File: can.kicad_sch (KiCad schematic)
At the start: 3 parts, among them J6 Conn_01x02, U6 TCAN334

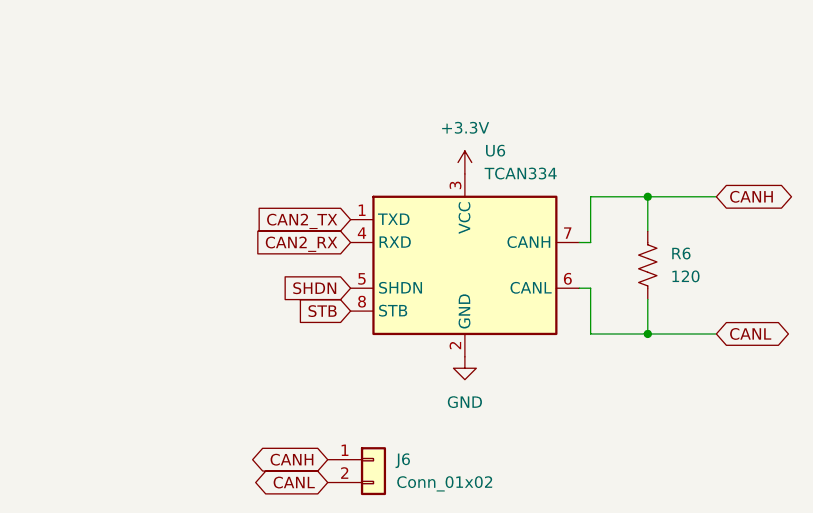
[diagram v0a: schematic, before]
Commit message: added load switches
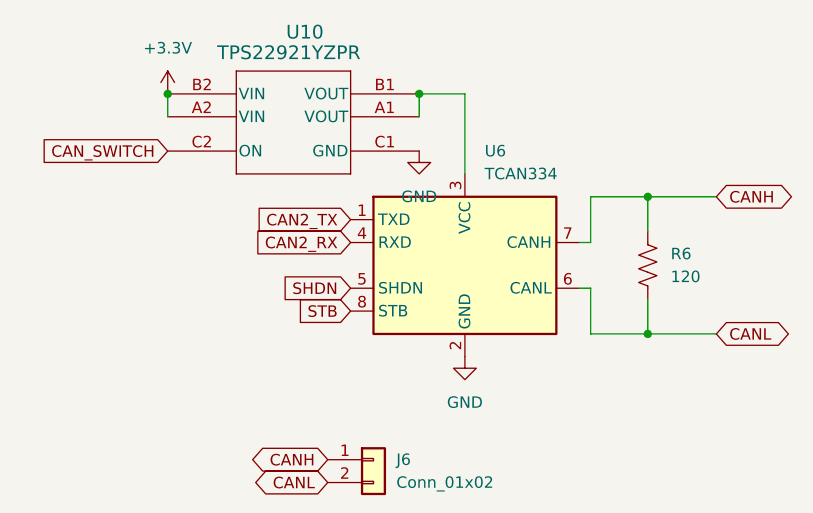
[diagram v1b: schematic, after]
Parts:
- added U10: TPS22921YZPR, YZP6, symbol TPS22921:TPS22921YZPR
- J6: footprint (none) -> Connector_JST:JST_SH_BM02B-SRSS-TB_1x02-1MP_P1.00mm_Vertical
- R6: footprint (none) -> Resistor_SMD:R_0402_1005Metric
- U6: footprint (none) -> footprints:DCN0008A_M
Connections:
- net +3.3V: now also U10.A2 (VIN), U10.B2 (VIN); no longer U6.3 (VCC)
- net GND: now also U10.C1 (GND)
- new net: U10.A1 (VOUT), U10.B1 (VOUT), U6.3 (VCC)
- new net CAN_SWITCH: U10.C2 (ON)
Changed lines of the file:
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@@
+	)
+	(junction
+		(at 29.21 35.56)
+		(diameter 0)
+		(color 0 0 0 0)
+	)
+	(junction
+		(at 57.15 35.56)
+		(diameter 0)
+		(color 0 0 0 0)
 	)
 	(junction
@@
 	(wire
 		(pts
+			(xy 57.15 35.56) (xy 57.15 38.1)
+		)
+		(stroke
+			(width 0)
+			(type default)
+		)
+	)
+	(wire
+		(pts
 			(xy 76.2 46.99) (xy 76.2 52.07)
 		)
@@
 	(wire
 		(pts
+			(xy 62.23 35.56) (xy 62.23 44.45)
+		)
+		(stroke
+			(width 0)
+			(type default)
+		)
+	)
+	(wire
+		(pts
+			(xy 57.15 35.56) (xy 62.23 35.56)
+		)
+		(stroke
+			(width 0)
+			(type default)
+		)
+	)
+	(wire
+		(pts
 			(xy 76.2 52.07) (xy 74.93 52.07)
 		)
@@
 		(pts
 			(xy 76.2 57.15) (xy 74.93 57.15)
+		)
+		(stroke
+			(width 0)
+			(type default)
+		)
+	)
+	(wire
+		(pts
+			(xy 29.21 35.56) (xy 29.21 38.1)
 		)
 		(stroke
@@
 		)
 	)
+	(global_label "CAN_SWITCH"
+		(shape input)
+		(at 29.21 41.91 180)
+		(fields_autoplaced yes)
+		(effects
+			(font
+				(size 1.27 1.27)
+			)
+			(justify right)
+		)
+		(property "Intersheetrefs" "${INTERSHEET_REFS}"
+			(at 14.7343 41.91 0)
+			(effects
+				(font
+					(size 1.27 1.27)
+				)
+				(justify right)
+				(hide yes)
+			)
+		)
+	)
 	(global_label "SHDN"
 		(shape input)
@@
 				)
 				(hide yes)
+			)
+		)
+	)
+	(symbol
+		(lib_id "power:GND")
+		(at 57.15 41.91 0)
+		(unit 1)
+		(exclude_from_sim no)
+		(in_bom yes)
+		(on_board yes)
+		(dnp no)
+		(fields_autoplaced yes)
+		(property "Reference" "#PWR060"
+			(at 57.15 48.26 0)
+			(effects
+				(font
+					(size 1.27 1.27)
+				)
+				(hide yes)
+			)
+		)
+		(property "Value" "GND"
+			(at 57.15 46.99 0)
+			(effects
+				(font
+					(size 1.27 1.27)
+				)
+			)
+		)
+		(property "Footprint" ""
+			(at 57.15 41.91 0)
+			(effects
+				(font
+					(size 1.27 1.27)
+				)
+				(hide yes)
+			)
+		)
+		(property "Datasheet" ""
+			(at 57.15 41.91 0)
+			(effects
+				(font
+					(size 1.27 1.27)
+				)
+				(hide yes)
+			)
+		)
+		(property "Description" "Power symbol creates a global label with name \"GND\" , ground"
+			(at 57.15 41.91 0)
+			(effects
+				(font
+					(size 1.27 1.27)
+				)
+				(hide yes)
+			)
+		)
+		(pin "1"
+		)
+		(instances
+			(project "RT1050"
+				(path "/dd9d031d-43a1-4442-b493-27451a14e0d9/1717ddd0-007d-45d1-b2d6-3a5f196579be"
+					(reference "#PWR060")
+					(unit 1)
+				)
 			)
 		)
@@
 			)
 		)
-		(property "Footprint" ""
+		(property "Footprint" "Resistor_SMD:R_0402_1005Metric"
 			(at 83.566 54.864 90)
 			(effects
@@
 				(path "/dd9d031d-43a1-4442-b493-27451a14e0d9/1717ddd0-007d-45d1-b2d6-3a5f196579be"
 					(reference "R6")
+					(unit 1)
+				)
+			)
+		)
+	)
+	(symbol
+		(lib_id "TPS22921:TPS22921YZPR")
+		(at 1.27 35.56 0)
+		(unit 1)
+		(exclude_from_sim no)
+		(in_bom yes)
+		(on_board yes)
+		(dnp no)
+		(property "Reference" "U10"
+			(at 44.45 28.702 0)
+			(effects
+				(font
+					(size 1.524 1.524)
+				)
+			)
+		)
+		(property "Value" "TPS22921YZPR"
+			(at 42.672 30.988 0)
+			(effects
+				(font
+					(size 1.524 1.524)
+				)
+			)
+		)
+		(property "Footprint" "YZP6"
+			(at 1.27 35.56 0)
+			(effects
+				(font
+					(size 1.27 1.27)
+					(italic yes)
+				)
+				(hide yes)
+			)
+		)
+		(property "Datasheet" "TPS22921YZPR"
+			(at 1.27 35.56 0)
+			(effects
+				(font
+					(size 1.27 1.27)
+					(italic yes)
+				)
+				(hide yes)
+			)
+		)
+		(property "Description" ""
+			(at 1.27 35.56 0)
+			(effects
+				(font
+					(size 1.27 1.27)
+				)
+				(hide yes)
+			)
+		)
+		(pin "A2"
+		)
+		(pin "A1"
+		)
+		(pin "B1"
+		)
+		(pin "C2"
+		)
+		(pin "C1"
+		)
+		(pin "B2"
+		)
+		(instances
+			(project ""
+				(path "/dd9d031d-43a1-4442-b493-27451a14e0d9/1717ddd0-007d-45d1-b2d6-3a5f196579be"
+					(reference "U10")
 					(unit 1)
 				)
@@
 			)
 		)
-		(property "Footprint" ""
+		(property "Footprint" "footprints:DCN0008A_M"
 			(at 62.23 67.31 0)
 			(effects
@@
 				(path "/dd9d031d-43a1-4442-b493-27451a14e0d9/1717ddd0-007d-45d1-b2d6-3a5f196579be"
 					(reference "U6")
+					(unit 1)
+				)
+			)
+		)
+	)
+	(symbol
+		(lib_id "power:+3.3V")
+		(at 29.21 35.56 0)
+		(unit 1)
+		(exclude_from_sim no)
+		(in_bom yes)
+		(on_board yes)
+		(dnp no)
+		(fields_autoplaced yes)
+		(property "Reference" "#PWR050"
+			(at 29.21 39.37 0)
+			(effects
+				(font
+					(size 1.27 1.27)
+				)
+				(hide yes)
+			)
+		)
+		(property "Value" "+3.3V"
+			(at 29.21 30.48 0)
+			(effects
+				(font
+					(size 1.27 1.27)
+				)
+			)
+		)
+		(property "Footprint" ""
+			(at 29.21 35.56 0)
+			(effects
+				(font
+					(size 1.27 1.27)
+				)
+				(hide yes)
+			)
+		)
+		(property "Datasheet" ""
+			(at 29.21 35.56 0)
+			(effects
+				(font
+					(size 1.27 1.27)
+				)
+				(hide yes)
+			)
+		)
+		(property "Description" "Power symbol creates a global label with name \"+3.3V\""
+			(at 29.21 35.56 0)
+			(effects
+				(font
+					(size 1.27 1.27)
+				)
+				(hide yes)
+			)
+		)
+		(pin "1"
+		)
+		(instances
+			(project "RT1050"
+				(path "/dd9d031d-43a1-4442-b493-27451a14e0d9/1717ddd0-007d-45d1-b2d6-3a5f196579be"
+					(reference "#PWR050")
 					(unit 1)
 				)
@@
 	)
 	(symbol
-		(lib_id "power:+3.3V")
-		(at 62.23 44.45 0)
-		(unit 1)
-		(exclude_from_sim no)
-		(in_bom yes)
-		(on_board yes)
-		(dnp no)
-		(fields_autoplaced yes)
-		(property "Reference" "#PWR050"
-			(at 62.23 48.26 0)
-			(effects
-				(font
-					(size 1.27 1.27)
-				)
-				(hide yes)
-			)
-		)
-		(property "Value" "+3.3V"
-			(at 62.23 39.37 0)
-			(effects
-				(font
-					(size 1.27 1.27)
-				)
-			)
-		)
-		(property "Footprint" ""
-			(at 62.23 44.45 0)
-			(effects
-				(font
-					(size 1.27 1.27)
-				)
-				(hide yes)
-			)
-		)
-		(property "Datasheet" ""
-			(at 62.23 44.45 0)
-			(effects
-				(font
-					(size 1.27 1.27)
-				)
-				(hide yes)
-			)
-		)
-		(property "Description" "Power symbol creates a global label with name \"+3.3V\""
-			(at 62.23 44.45 0)
-			(effects
-				(font
-					(size 1.27 1.27)
-				)
-				(hide yes)
-			)
-		)
-		(pin "1"
-		)
-		(instances
-			(project ""
-				(path "/dd9d031d-43a1-4442-b493-27451a14e0d9/1717ddd0-007d-45d1-b2d6-3a5f196579be"
-					(reference "#PWR050")
-					(unit 1)
-				)
-			)
-		)
-	)
-	(symbol
 		(lib_id "Connector_Generic:Conn_01x02")
 		(at 52.07 76.2 0)
@@
 			)
 		)
-		(property "Footprint" ""
+		(property "Footprint" "Connector_JST:JST_SH_BM02B-SRSS-TB_1x02-1MP_P1.00mm_Vertical"
 			(at 52.07 76.2 0)
 			(effects
